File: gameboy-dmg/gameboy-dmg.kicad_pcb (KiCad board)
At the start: 2 copper layers, 82.5 x 77.5 mm, 71 parts, among them J1 Conn_01x02, J2 Conn_01x02, J3 Conn_01x08, J4 Conn_01x02, J5 Raspberry_Pi_2_3, J6 Conn_01x09, J7 USB_B_Micro, J8 Conn_01x02, SW1 SW_DIP_x01, U1 MCP23017_SO, U2 TP4056, U3 FS312F-G, U4 FS8205, U5 MT3608

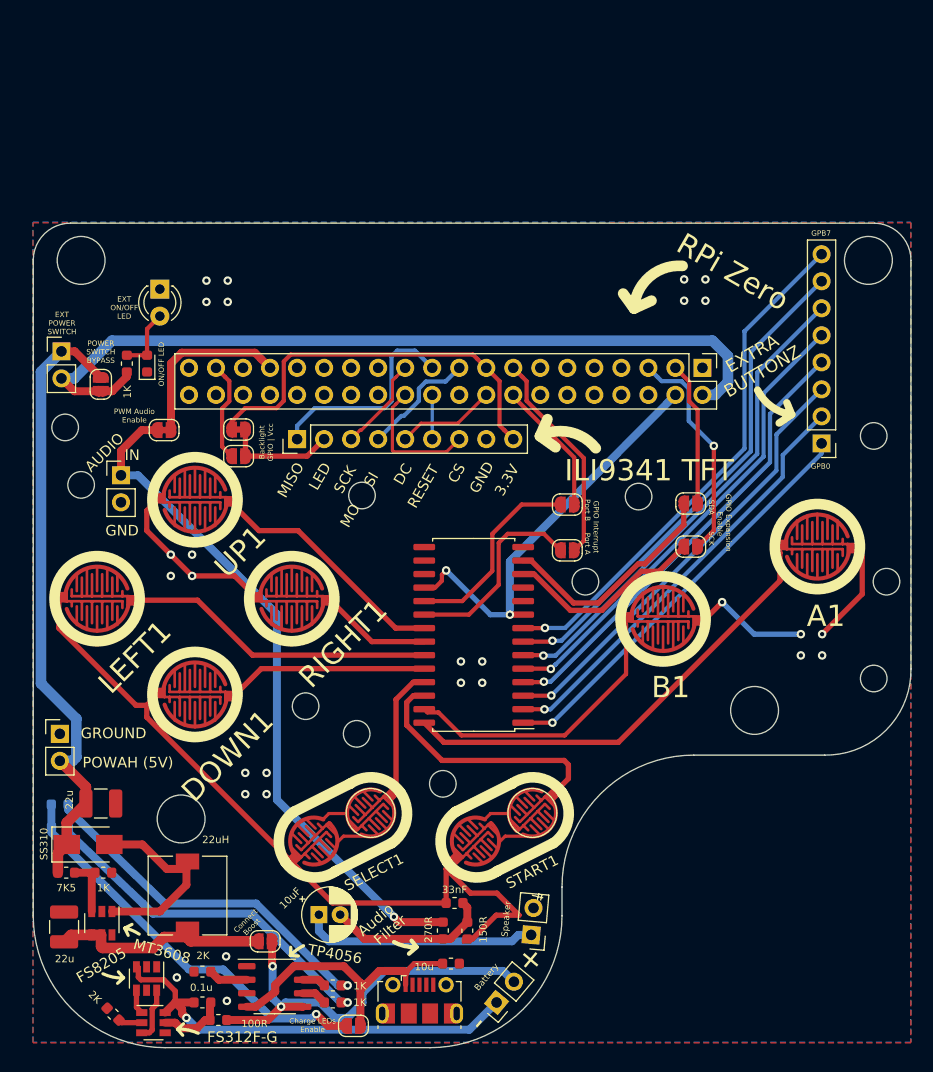
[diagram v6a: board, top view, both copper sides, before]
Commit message: Moved buttons and audio to individual sheets and added audio amp
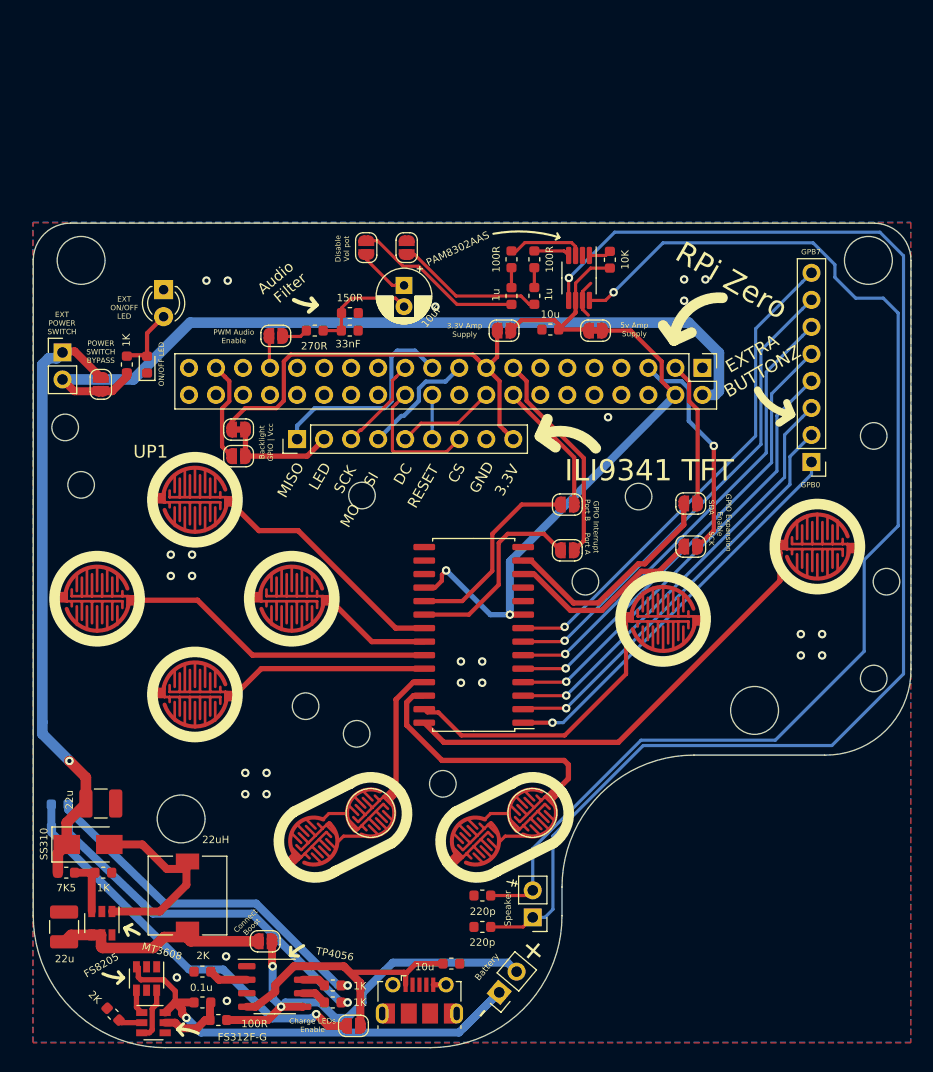
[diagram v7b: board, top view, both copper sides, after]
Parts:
- removed J2, J4: Conn_01x02, Connector_PinHeader_2.54mm:PinHeader_1x02_P2.54mm_Vertical
- added C10: 220p, Capacitor_SMD:C_0603_1608Metric, F.Cu at (165.2, 125.2)
- added C11: 220p, Capacitor_SMD:C_0603_1608Metric, F.Cu at (165.2, 122.2)
- added C7: 1u, Capacitor_SMD:C_0603_1608Metric, F.Cu at (167.9, 65.8)
- added C8: 1u, Capacitor_SMD:C_0603_1608Metric, F.Cu at (170.1, 65.8)
- added C9: 10u, Capacitor_SMD:C_0603_1608Metric, F.Cu at (171.6, 69.0)
- added JP10: SolderJumper_2_Open, Jumper:SolderJumper-2_P1.3mm_Open_RoundedPad1.0x1.5mm, F.Cu at (154.3, 61.3)
- added JP12: SolderJumper_2_Open, Jumper:SolderJumper-2_P1.3mm_Open_RoundedPad1.0x1.5mm, F.Cu at (167.2, 69.1)
- added JP13: SolderJumper_2_Bridged, Jumper:SolderJumper-2_P1.3mm_Bridged_RoundedPad1.0x1.5mm, F.Cu at (175.8, 69.1)
- added JP14: SolderJumper_2_Open, Jumper:SolderJumper-2_P1.3mm_Open_RoundedPad1.0x1.5mm, F.Cu at (158.1, 61.3)
- added R11: 100R, Resistor_SMD:R_0603_1608Metric, F.Cu at (167.9, 62.4)
- added R12: 100R, Resistor_SMD:R_0603_1608Metric, F.Cu at (170.1, 62.4)
- added R13: 10K, Resistor_SMD:R_0603_1608Metric, F.Cu at (177.2, 62.4)
- added U6: PAM8302AAS, Package_SO:MSOP-8_3x3mm_P0.65mm, F.Cu at (174.3, 64.2)
- JP1: value SolderJumper_2_Bridged -> SolderJumper_2_Open; footprint Jumper:SolderJumper-2_P1.3mm_Bridged_RoundedPad1.0x1.5mm -> Jumper:SolderJumper-2_P1.3mm_Open_RoundedPad1.0x1.5mm
- R1: value 270R -> 1K
- R2: value 150R -> 270R
- R3: value 1K -> 150R
- moved R1 60.9 mm to (131.8, 72.3)
- moved C2 59.7 mm to (157.8, 64.8), turned to 270 degrees
- moved R2 58.2 mm to (149.5, 69.1), turned to 180 degrees
- moved C1 54.7 mm to (152.8, 69.1), turned to 0 degrees
- moved R3 21.5 mm to (152.8, 67.5), turned to 180 degrees
- moved JP1 13.7 mm to (145.8, 69.6), turned to 0 degrees
- moved J3 1.99 mm to (196.2, 81.5)
- moved J1 1.66 mm to (169.9, 124.2), turned to 180 degrees
- moved J8 0.98 mm to (166.8, 131.3)
- moved D2 0.35 mm to (135.2, 65.2)
- moved SW1 0.14 mm to (125.8, 71.2)
- moved D1 0.10 mm to (133.7, 72.3)
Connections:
- net BOOST_5V renamed /TP4056_LIPO_BOOST/5V_BOOST
- C2 pad 1: /AUDIO_OUT -> Net-(C2-Pad1)
- J1 pad 1: /AUDIO_OUT -> Net-(C10-Pad1)
- J1 pad 2: GND -> Net-(C11-Pad1)
- JP1 pad 2: /PWM_IN -> /PWM_AUDIO_OUT
- R1 pad 1: Net-(C1-Pad1) -> +5V
- R1 pad 2: /PWM_IN -> Net-(D1-Pad2)
- R2 pad 1: GND -> Net-(C1-Pad1)
- R2 pad 2: Net-(C1-Pad1) -> /PWM_AUDIO_OUT
- R3 pad 1: +5V -> GND
- R3 pad 2: Net-(D1-Pad2) -> Net-(C1-Pad1)
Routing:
- net Net-(C10-Pad1): track 0.00 -> 128.3 mm, vias 0 -> 1
- net Net-(C11-Pad1): track 0.00 -> 114.7 mm, vias 0 -> 1
- net GND: track 108.1 -> 4.75 mm
- net /PWM_IN: track 64.4 -> 0.00 mm, vias 1 -> 0
- net /AUDIO_OUT: track 22.1 -> 0.00 mm
- net /audio/Audio_Vdd: track 0.00 -> 17.2 mm
- net Net-(C7-Pad1): track 0.00 -> 16.1 mm
- net Net-(C8-Pad2): track 0.00 -> 13.9 mm
- net Net-(J5-Pad33): track 16.6 -> 3.35 mm
- net +5V: track 116.8 -> 127.6 mm
- net Net-(R11-Pad1): track 0.00 -> 7.34 mm
- net /TP4056_LIPO_BOOST/BAT-: track 41.9 -> 47.4 mm
- net Net-(C1-Pad1): track 15.7 -> 10.4 mm
- net Net-(C2-Pad1): track 0.00 -> 5.01 mm
- net +3V3: track 37.7 -> 41.6 mm
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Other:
- board text added: "3.3V Amp Supply"
- board text added: "5v Amp Supply"
- board text added: "Disable Vol pot"
- board text removed: "AUDIO"
- board text removed: "GROUND"
- board text removed: "IN"
- board text removed: "POWAH (5V)"

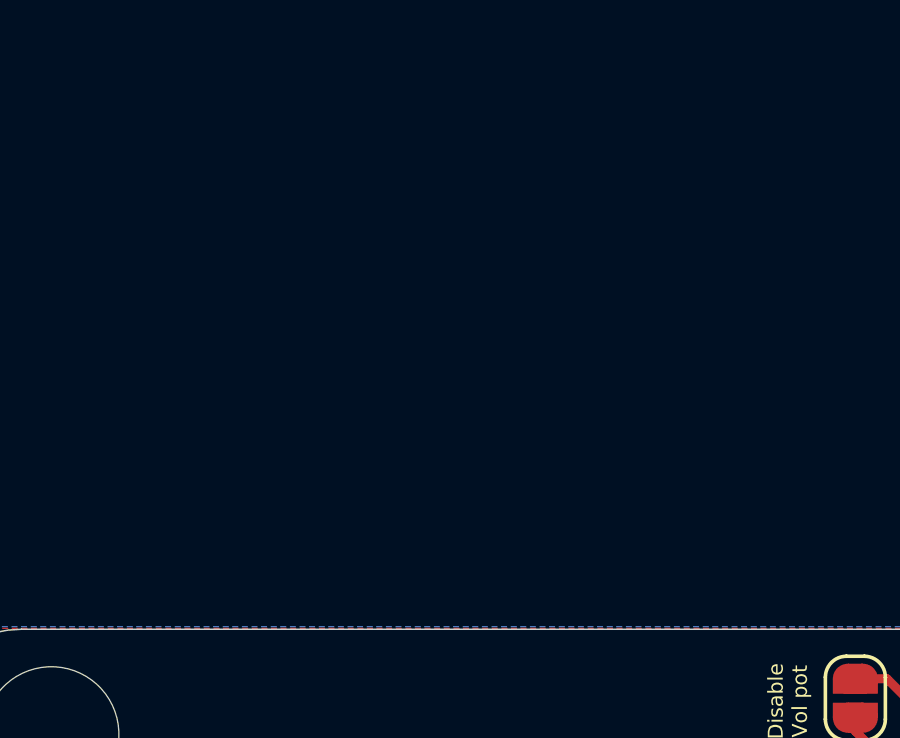
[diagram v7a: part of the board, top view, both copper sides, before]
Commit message: Added unroputed and unchecked horizontal vol pot
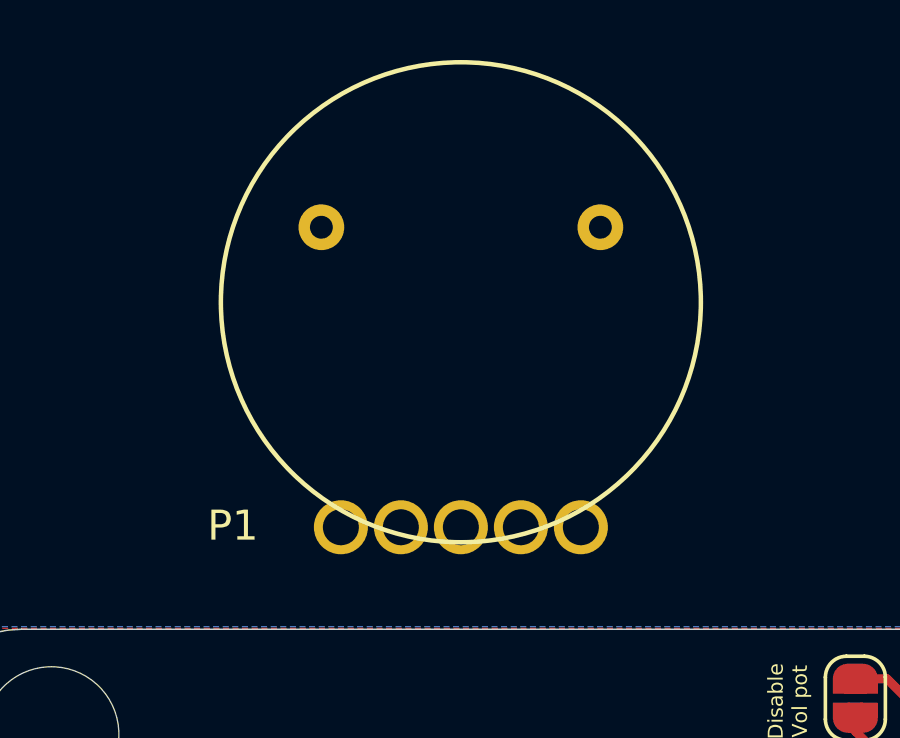
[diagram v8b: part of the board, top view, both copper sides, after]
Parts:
- added P1: RK10J_POT, pad:R503_POT, F.Cu at (141.2, 55.6)
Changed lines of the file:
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@@
     (tracks 485)
     (zones 0)
-    (modules 82)
-    (nets 94)
+    (modules 83)
+    (nets 96)
   )
   (page A4)
@@
   )
   (setup
-    (last_trace_width 0.75)
+    (last_trace_width 0.3)
     (user_trace_width 0.3)
     (user_trace_width 0.4)
@@
   (net 92 "Net-(C2-Pad1)")
   (net 93 "Net-(C8-Pad2)")
+  (net 94 "Net-(P1-Pad3)")
+  (net 95 "Net-(P1-Pad5)")
   (net_class Default "This is the default net class."
     (clearance 0.2)
@@
     (add_net "Net-(J7-Pad3)")
     (add_net "Net-(J7-Pad4)")
+    (add_net "Net-(P1-Pad3)")
+    (add_net "Net-(P1-Pad5)")
     (add_net "Net-(R10-Pad1)")
     (add_net "Net-(R11-Pad1)")
@@
       ))
   )
+  (module pad:R503_POT (layer F.Cu)
+    (at 141.15 55.6)
+    (fp_text reference P1 (at -7.6 -0.05) (layer F.SilkS)
+      (effects (font (size 1 1) (thickness 0.15)))
+    )
+    (fp_text value RK10J_POT (at -0.05 -5.45) (layer F.Fab)
+      (effects (font (size 1 1) (thickness 0.15)))
+    )
+    (fp_circle (center 0 -7.5) (end 0 0.5) (layer F.SilkS) (width 0.15))
+    (pad 1 thru_hole circle (at -4 0) (size 1.8 1.8) (drill 1.2) (layers *.Cu *.Mask)
+      (net 93 "Net-(C8-Pad2)"))
+    (pad ~ thru_hole circle (at -4.65 -10) (size 1.524 1.524) (drill 0.762) (layers *.Cu *.Mask))
+    (pad 2 thru_hole circle (at -2 0) (size 1.8 1.8) (drill 1.2) (layers *.Cu *.Mask)
+      (net 92 "Net-(C2-Pad1)"))
+    (pad 3 thru_hole circle (at 0 0) (size 1.8 1.8) (drill 1.2) (layers *.Cu *.Mask)
+      (net 94 "Net-(P1-Pad3)"))
+    (pad 4 thru_hole circle (at 2 0) (size 1.8 1.8) (drill 1.2) (layers *.Cu *.Mask)
+      (net 82 "Net-(C7-Pad1)"))
+    (pad 5 thru_hole circle (at 4 0) (size 1.8 1.8) (drill 1.2) (layers *.Cu *.Mask)
+      (net 95 "Net-(P1-Pad5)"))
+    (pad ~ thru_hole circle (at 4.65 -10) (size 1.524 1.524) (drill 0.762) (layers *.Cu *.Mask))
+  )
   (gr_text "Disable\nVol pot" (at 152.05 61.4 90) (layer F.SilkS)
     (effects (font (size 0.5 0.5) (thickness 0.1)))
@@
     (connect_pads (clearance 0.4))
     (min_thickness 0.254)
-    (fill yes (arc_segments 32) (thermal_gap 0.508) (thermal_bridge_width 0.508))
+    (fill (arc_segments 32) (thermal_gap 0.508) (thermal_bridge_width 0.508))
     (polygon
       (pts
@@
     (connect_pads (clearance 0.4))
     (min_thickness 0.254)
-    (fill yes (arc_segments 32) (thermal_gap 0.508) (thermal_bridge_width 0.508) (smoothing chamfer))
+    (fill (arc_segments 32) (thermal_gap 0.508) (thermal_bridge_width 0.508) (smoothing chamfer))
     (polygon
       (pts
